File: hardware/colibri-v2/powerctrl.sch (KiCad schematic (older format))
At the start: 48 parts

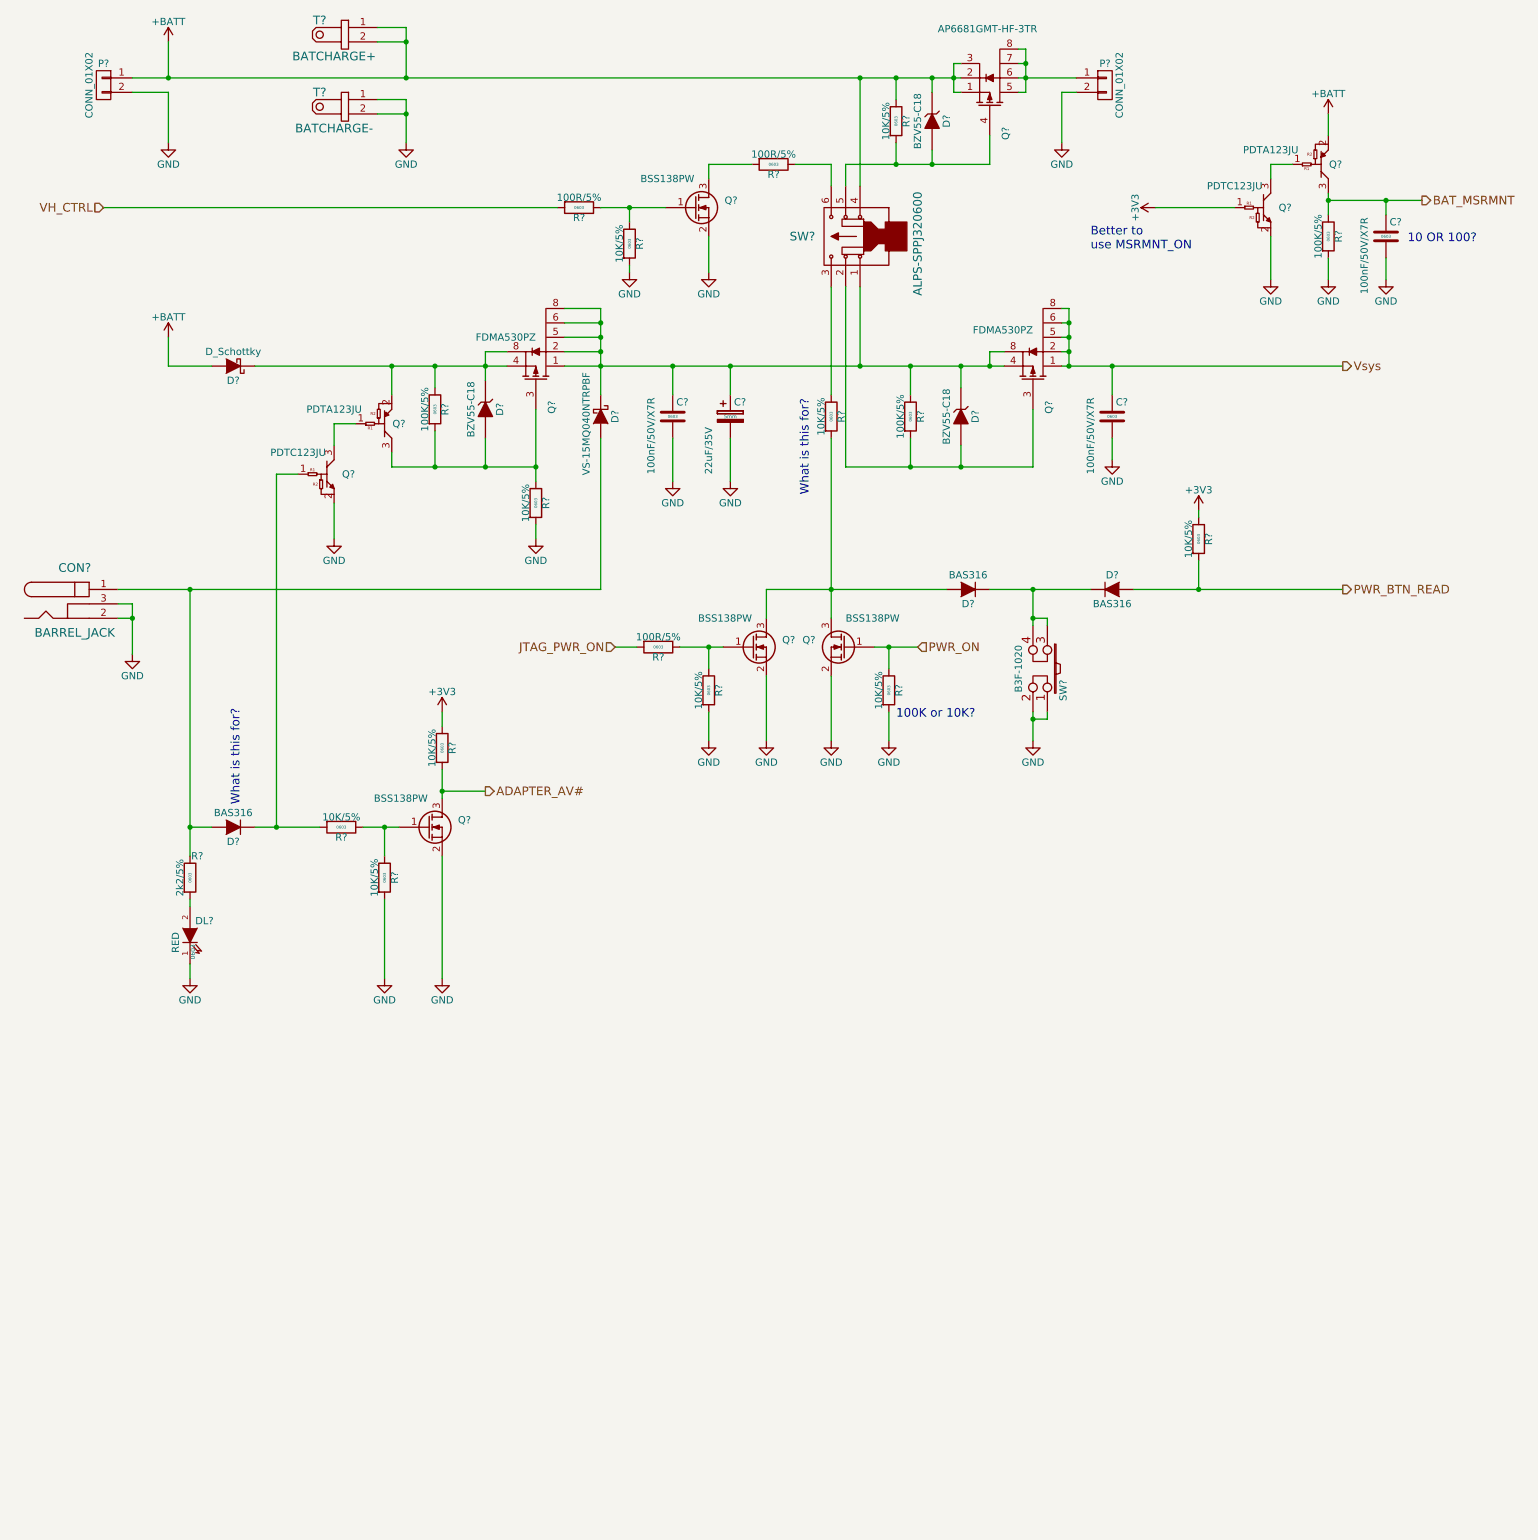
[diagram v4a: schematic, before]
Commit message: Work on power controll, buttons
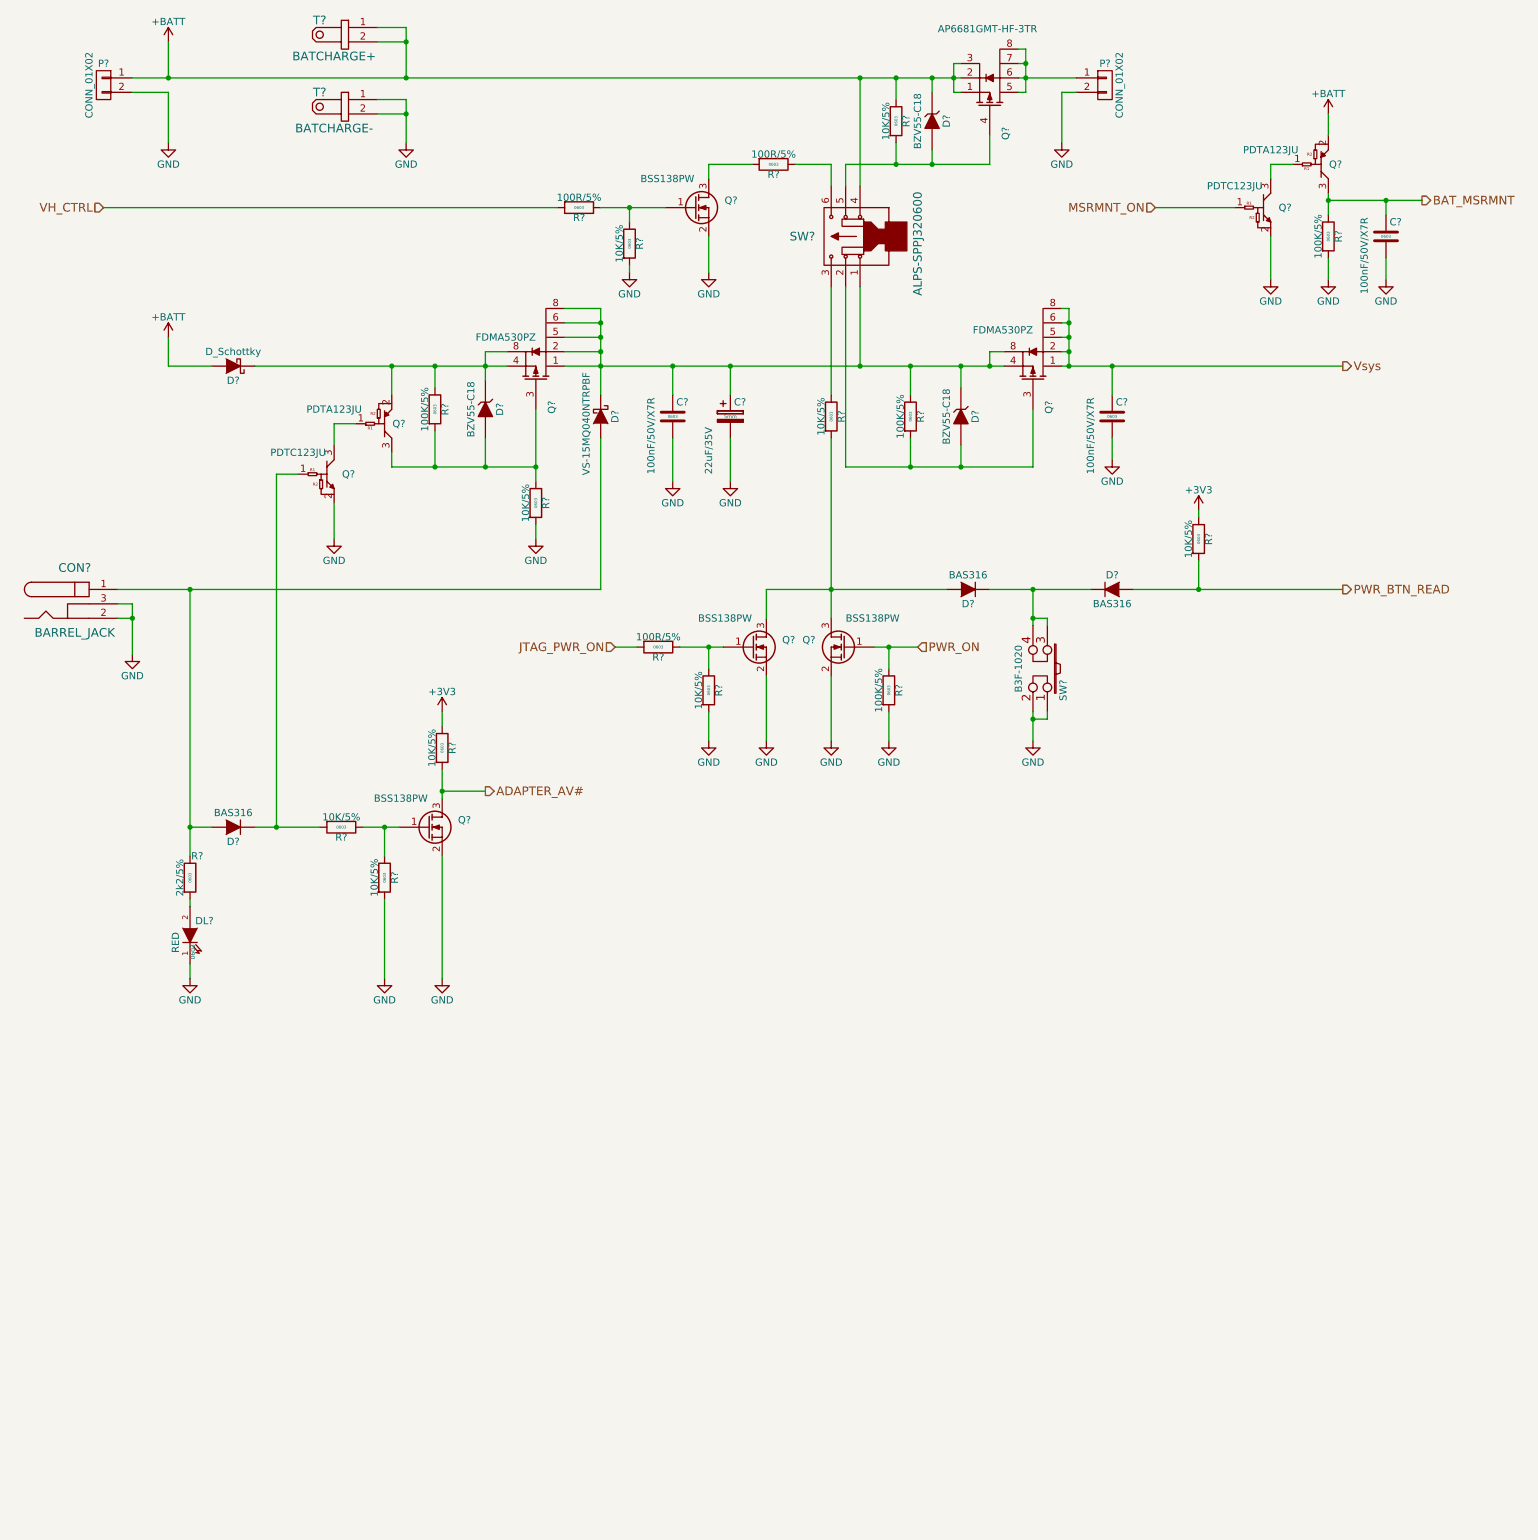
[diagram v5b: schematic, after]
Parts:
- removed R?: 10K/5%, Resistors_SMD:R_0603, symbol R_SMT
- added R?: 100K/5%, Resistors_SMD:R_0603, symbol R_SMT
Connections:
- net +3V3: no longer Q?.1
- net GND: now also R?.2
- net PWR_ON: now also R?.1
- new net MSRMNT_ON: Q?.1
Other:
- note removed: "10 OR 100?"
- note removed: "100K or 10K?"
- note removed: "Better to\nuse MSRMNT_ON"
- note removed: "What is this for?"
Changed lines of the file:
@@
-$EndComp
-$Comp
-L R_SMT R?
-U 1 1 5650C7BE
-P 6650 5300
-F 0 "R?" V 6720 5300 50  0000 C CNN
-F 1 "10K/5%" V 6580 5300 50  0000 C CNN
-F 2 "Resistors_SMD:R_0603" V 6800 5300 30  0001 C CNN
-F 3 "" V 6730 5300 30  0000 C CNN
-F 4 "0603" V 6650 5300 20  0000 C CNN "SMT"
-F 5 "9331700" V 6850 5300 30  0001 C CNN "Part"
-F 6 "Farnell" V 6900 5300 30  0001 C CNN "Provider"
-	1    6650 5300
-	1    0    0    -1
 $EndComp
 $Comp
@@
 	1    0    0    -1
 $EndComp
-Text Notes 6100 3950 1    60   ~ 0
-What is this for?
-Text Notes 6700 5500 0    60   ~ 0
-100K or 10K?
-Text Notes 2150 6100 1    60   ~ 0
-What is this for?
 Wire Wire Line
 	3100 1200 3300 1200
@@
 Wire Wire Line
 	10100 2300 10100 2450
-Text Notes 10250 2200 0    60   ~ 0
-10 OR 100?
-$Comp
-L +3V3 #PWR?
-U 1 1 565248B4
-P 8500 1950
-F 0 "#PWR?" H 8500 1800 50  0001 C CNN
-F 1 "+3V3" H 8500 2090 50  0000 C CNN
-F 2 "" H 8500 1950 60  0000 C CNN
-F 3 "" H 8500 1950 60  0000 C CNN
-	1    8500 1950
-	0    -1   -1   0
-$EndComp
 Wire Wire Line
 	8500 1950 9050 1950
-Text Notes 8050 2250 0    60   ~ 0
-Better to\nuse MSRMNT_ON
 Wire Wire Line
 	4000 2950 3850 2950
@@
 	4400 2650 4650 2650
 Connection ~ 4650 2750
+$Comp
+L R_SMT R?
+U 1 1 5653DB72
+P 6650 5300
+F 0 "R?" V 6720 5300 50  0000 C CNN
+F 1 "100K/5%" V 6580 5300 50  0000 C CNN
+F 2 "Resistors_SMD:R_0603" V 6800 5300 30  0001 C CNN
+F 3 "" V 6730 5300 30  0000 C CNN
+F 4 "0603" V 6650 5300 20  0000 C CNN "SMT"
+F 5 "9233628" V 6850 5300 30  0001 C CNN "Part"
+F 6 "Farnell" V 6900 5300 30  0001 C CNN "Provider"
+	1    6650 5300
+	1    0    0    -1
+$EndComp
+Text HLabel 8500 1950 0    60   Input ~ 0
+MSRMNT_ON
 $EndSCHEMATC

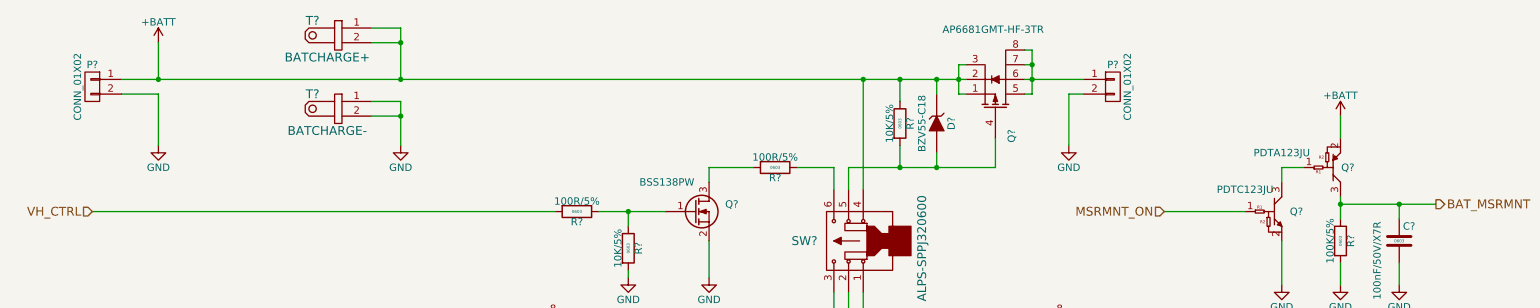
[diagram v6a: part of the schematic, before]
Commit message: Added XT60 connectors to battery and mottors
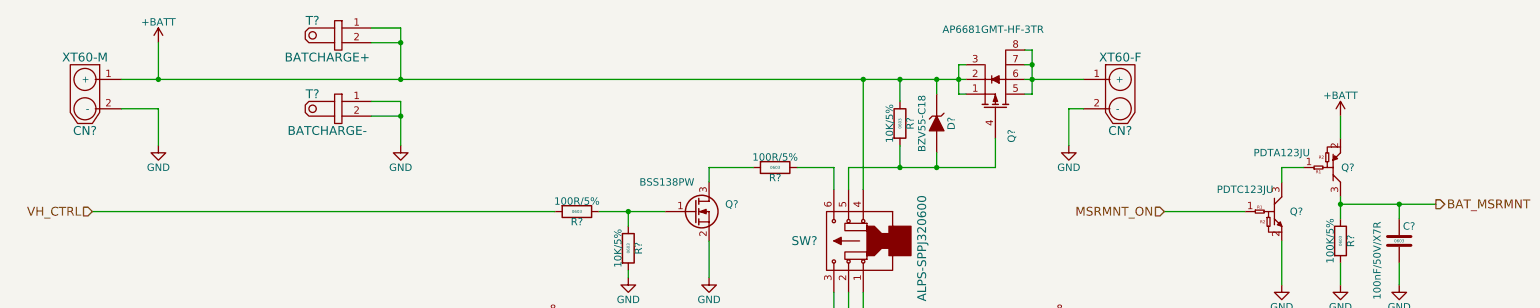
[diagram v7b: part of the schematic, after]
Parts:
- removed P? (x2): CONN_01X02, symbol CONN_01X02
- added CN?: XT60-M, Sigmadrone:xt60, symbol XT60
- added CN?: XT60-F, Sigmadrone:xt60, symbol XT60
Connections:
- net +BATT: now also CN?.1 (+)
- net GND: now also CN?.2 (-), CN?.2 (-)
- net at Q?.5 (D), Q?.6 (D), Q?.7 (D)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: now also CN?.1 (+)
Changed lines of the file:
@@
 $EndDescr
-$Comp
-L CONN_01X02 P?
-U 1 1 55962775
-P 1200 1100
-F 0 "P?" H 1200 1250 50  0000 C CNN
-F 1 "CONN_01X02" V 1300 1100 50  0000 C CNN
-F 2 "" H 1200 1100 60  0001 C CNN
-F 3 "" H 1200 1100 60  0000 C CNN
-	1    1200 1100
-	-1   0    0    -1
-$EndComp
-$Comp
-L CONN_01X02 P?
-U 1 1 559627DB
-P 8150 1100
-F 0 "P?" H 8150 1250 50  0000 C CNN
-F 1 "CONN_01X02" V 8250 1100 50  0000 C CNN
-F 2 "" H 8150 1100 60  0001 C CNN
-F 3 "" H 8150 1100 60  0000 C CNN
-	1    8150 1100
-	1    0    0    -1
-$EndComp
 $Comp
 L GND #PWR?
@@
 Connection ~ 1650 1050
 Wire Wire Line
-	7950 1150 7850 1150
-Wire Wire Line
-	7850 1150 7850 1500
-Wire Wire Line
-	1400 1150 1650 1150
-Wire Wire Line
-	1650 1150 1650 1500
+	1400 1250 1650 1250
+Wire Wire Line
+	1650 1250 1650 1500
 Wire Wire Line
 	2250 6250 2700 6250
@@
 BAT_MSRMNT
 Wire Wire Line
-	10350 1900 9700 1900
+	9700 1900 10350 1900
 Connection ~ 9700 1900
 $Comp
@@
 Text HLabel 8500 1950 0    60   Input ~ 0
 MSRMNT_ON
+$Comp
+L XT60 CN?
+U 1 1 566008A4
+P 1150 1150
+F 0 "CN?" H 1150 1400 60  0000 C CNN
+F 1 "XT60-M" H 1150 900 60  0000 C CNN
+F 2 "Sigmadrone:xt60" H 1150 850 60  0001 C CNN
+F 3 "" H 1150 1300 60  0000 C CNN
+	1    1150 1150
+	-1   0    0    1
+$EndComp
+$Comp
+L XT60 CN?
+U 1 1 56600C8C
+P 8200 1150
+F 0 "CN?" H 8200 1400 60  0000 C CNN
+F 1 "XT60-F" H 8200 900 60  0000 C CNN
+F 2 "Sigmadrone:xt60" H 8200 850 60  0001 C CNN
+F 3 "" H 8200 1300 60  0000 C CNN
+	1    8200 1150
+	1    0    0    1
+$EndComp
+Wire Wire Line
+	7950 1250 7850 1250
+Wire Wire Line
+	7850 1250 7850 1500
 $EndSCHEMATC
